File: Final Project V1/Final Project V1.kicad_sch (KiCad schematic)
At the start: 51 parts, among them J1 39299043, J2 Conn_02x03_Counter_Clockwise, J3 Conn_02x02_Counter_Clockwise, J4 Conn_02x01, J5 Conn_02x01, J7 Conn_02x01, J8 75867-132LF, J9 10056845-110LF, Q1 SS8050-G, Q2 SS8050-G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

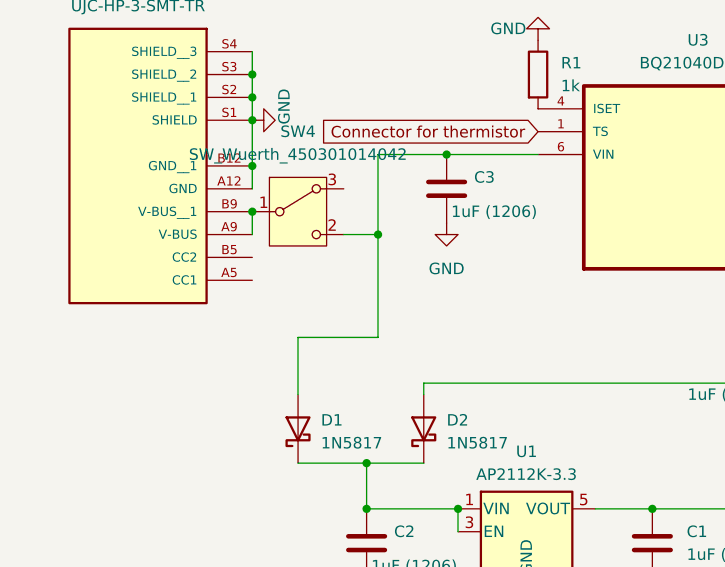
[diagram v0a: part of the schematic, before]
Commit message: Added resistors to control channel on USB-C cause I am a silly goose and didn't do that before
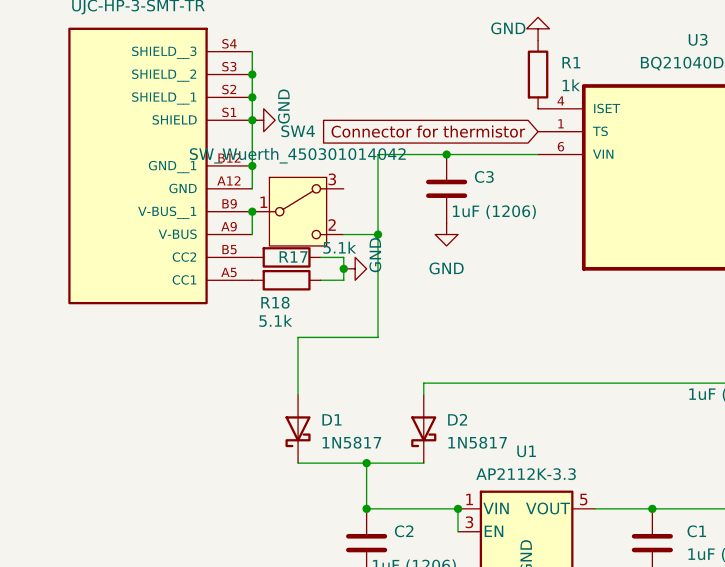
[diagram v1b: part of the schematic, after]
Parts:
- added R17, R18: 5.1k, Resistor_SMD:R_0805_2012Metric_Pad1.20x1.40mm_HandSolder, symbol Device:R
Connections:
- net GND: now also R17.1, R18.1
- net at USB-C1.A5 (CC1): now also R18.2
- net at USB-C1.B5 (CC2): now also R17.2
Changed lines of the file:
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@@
 	)
 	(junction
+		(at 44.45 40.64)
+		(diameter 0)
+		(color 0 0 0 0)
+	)
+	(junction
 		(at 179.07 60.96)
 		(diameter 0)
@@
 	(wire
 		(pts
+			(xy 44.45 41.91) (xy 44.45 40.64)
+		)
+		(stroke
+			(width 0)
+			(type default)
+		)
+	)
+	(wire
+		(pts
 			(xy 199.39 58.42) (xy 201.93 58.42)
 		)
@@
 	(wire
 		(pts
+			(xy 41.91 39.37) (xy 44.45 39.37)
+		)
+		(stroke
+			(width 0)
+			(type default)
+		)
+	)
+	(wire
+		(pts
 			(xy 228.6 74.93) (xy 228.6 80.01)
 		)
@@
 	(wire
 		(pts
+			(xy 41.91 41.91) (xy 44.45 41.91)
+		)
+		(stroke
+			(width 0)
+			(type default)
+		)
+	)
+	(wire
+		(pts
 			(xy 39.37 48.26) (xy 39.37 54.61)
 		)
@@
 	(wire
 		(pts
+			(xy 44.45 39.37) (xy 44.45 40.64)
+		)
+		(stroke
+			(width 0)
+			(type default)
+		)
+	)
+	(wire
+		(pts
 			(xy 243.84 146.05) (xy 246.38 146.05)
 		)
@@
 	)
 	(symbol
+		(lib_id "Device:R")
+		(at 38.1 41.91 270)
+		(unit 1)
+		(exclude_from_sim no)
+		(in_bom yes)
+		(on_board yes)
+		(dnp no)
+		(property "Reference" "R18"
+			(at 36.83 44.45 90)
+			(effects
+				(font
+					(size 1.27 1.27)
+				)
+			)
+		)
+		(property "Value" "5.1k"
+			(at 36.83 46.482 90)
+			(effects
+				(font
+					(size 1.27 1.27)
+				)
+			)
+		)
+		(property "Footprint" "Resistor_SMD:R_0805_2012Metric_Pad1.20x1.40mm_HandSolder"
+			(at 38.1 40.132 90)
+			(effects
+				(font
+					(size 1.27 1.27)
+				)
+				(hide yes)
+			)
+		)
+		(property "Datasheet" "~"
+			(at 38.1 41.91 0)
+			(effects
+				(font
+					(size 1.27 1.27)
+				)
+				(hide yes)
+			)
+		)
+		(property "Description" "Resistor"
+			(at 38.1 41.91 0)
+			(effects
+				(font
+					(size 1.27 1.27)
+				)
+				(hide yes)
+			)
+		)
+		(pin "1"
+		)
+		(pin "2"
+		)
+		(instances
+			(project "Final Project V1"
+				(path "/ac3e449f-fc44-4702-b75e-43cfa6f85799"
+					(reference "R18")
+					(unit 1)
+				)
+			)
+		)
+	)
+	(symbol
 		(lib_id "power:GND")
 		(at 274.32 114.3 0)
@@
 	)
 	(symbol
+		(lib_id "Device:R")
+		(at 38.1 39.37 270)
+		(unit 1)
+		(exclude_from_sim no)
+		(in_bom yes)
+		(on_board yes)
+		(dnp no)
+		(property "Reference" "R17"
+			(at 38.862 39.37 90)
+			(effects
+				(font
+					(size 1.27 1.27)
+				)
+			)
+		)
+		(property "Value" "5.1k"
+			(at 43.942 38.354 90)
+			(effects
+				(font
+					(size 1.27 1.27)
+				)
+			)
+		)
+		(property "Footprint" "Resistor_SMD:R_0805_2012Metric_Pad1.20x1.40mm_HandSolder"
+			(at 38.1 37.592 90)
+			(effects
+				(font
+					(size 1.27 1.27)
+				)
+				(hide yes)
+			)
+		)
+		(property "Datasheet" "~"
+			(at 38.1 39.37 0)
+			(effects
+				(font
+					(size 1.27 1.27)
+				)
+				(hide yes)
+			)
+		)
+		(property "Description" "Resistor"
+			(at 38.1 39.37 0)
+			(effects
+				(font
+					(size 1.27 1.27)
+				)
+				(hide yes)
+			)
+		)
+		(pin "1"
+		)
+		(pin "2"
+		)
+		(instances
+			(project "Final Project V1"
+				(path "/ac3e449f-fc44-4702-b75e-43cfa6f85799"
+					(reference "R17")
+					(unit 1)
+				)
+			)
+		)
+	)
+	(symbol
 		(lib_id "power:GND")
 		(at 64.77 77.47 0)
@@
 					(unit 1)
 				)
+			)
+		)
+	)
+	(symbol
+		(lib_id "power:GND")
+		(at 44.45 40.64 90)
+		(unit 1)
+		(exclude_from_sim no)
+		(in_bom yes)
+		(on_board yes)
+		(dnp no)
+		(property "Reference" "#PWR022"
+			(at 50.8 40.64 0)
+			(effects
+				(font
+					(size 1.27 1.27)
+				)
+				(hide yes)
+			)
+		)
+		(property "Value" "GND"
+			(at 48.006 39.116 0)
+			(effects
+				(font
+					(size 1.27 1.27)
+				)
+			)
+		)
+		(property "Footprint" ""
+			(at 44.45 40.64 0)
+			(effects
+				(font
+					(size 1.27 1.27)
+				)
+				(hide yes)
+			)
+		)
+		(property "Datasheet" ""
+			(at 44.45 40.64 0)
+			(effects
+				(font
+					(size 1.27 1.27)
+				)
+				(hide yes)
+			)
+		)
+		(property "Description" "Power symbol creates a global label with name \"GND\" , ground"
+			(at 44.45 40.64 0)
+			(effects
+				(font
+					(size 1.27 1.27)
+				)
+				(hide yes)
+			)
+		)
+		(pin "1"
+		)
+		(instances
+			(project "Final Project V1"
+				(path "/ac3e449f-fc44-4702-b75e-43cfa6f85799"
+					(reference "#PWR022")
+					(unit 1)
+				)

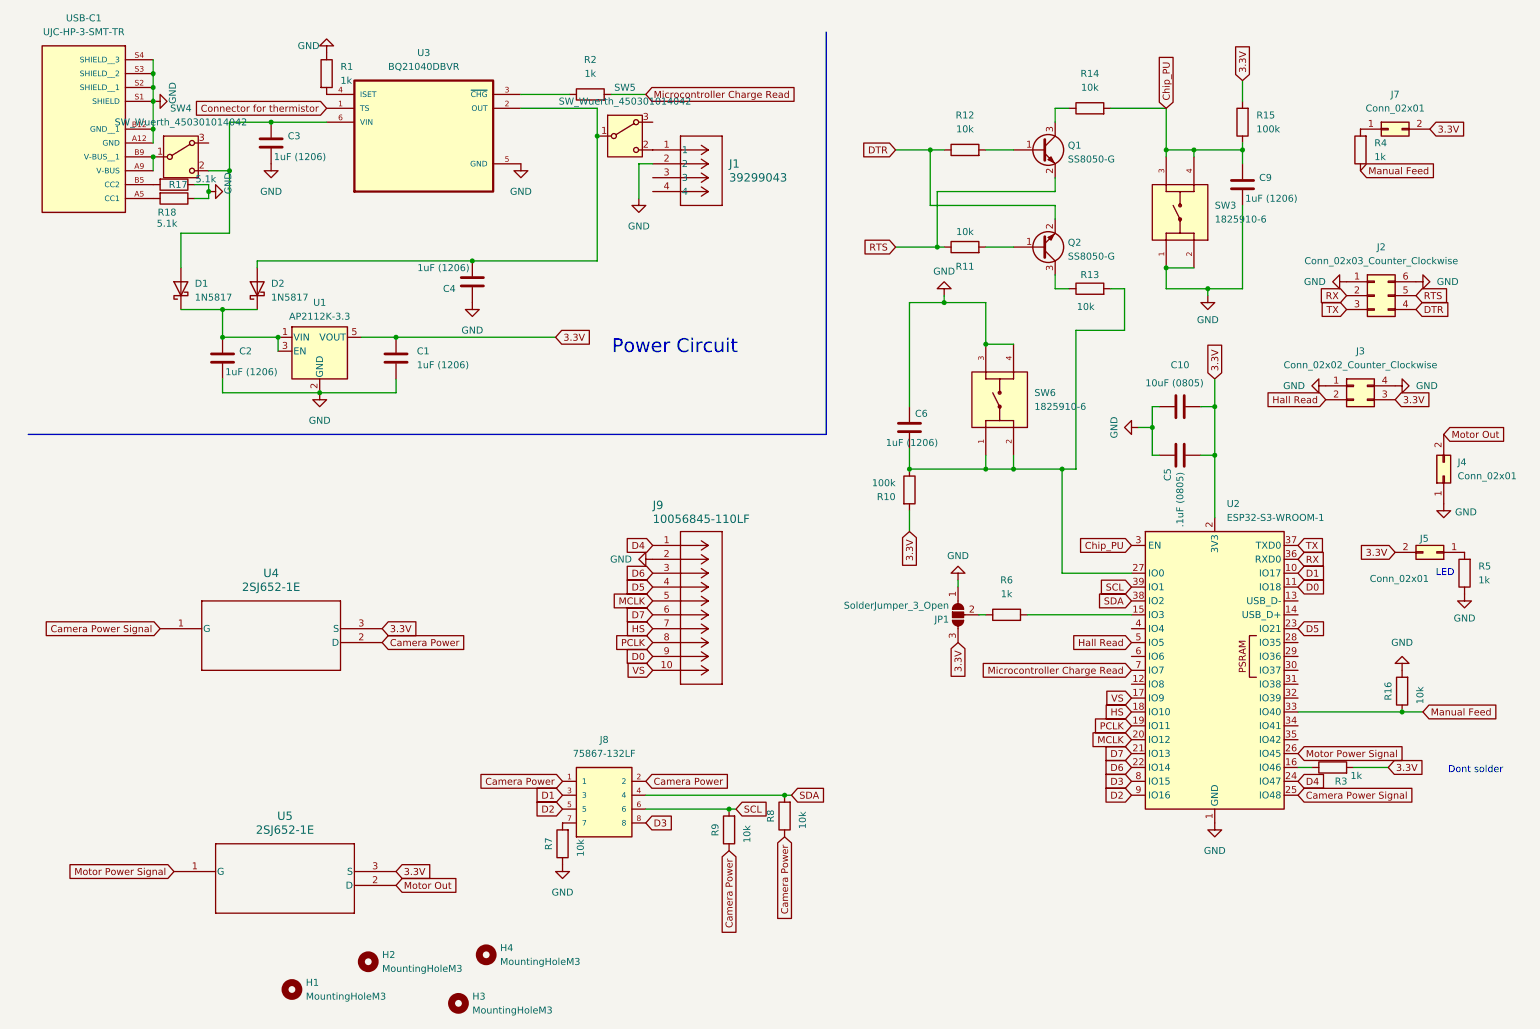
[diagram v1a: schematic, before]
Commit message: V4 Schematic. Will work with V3
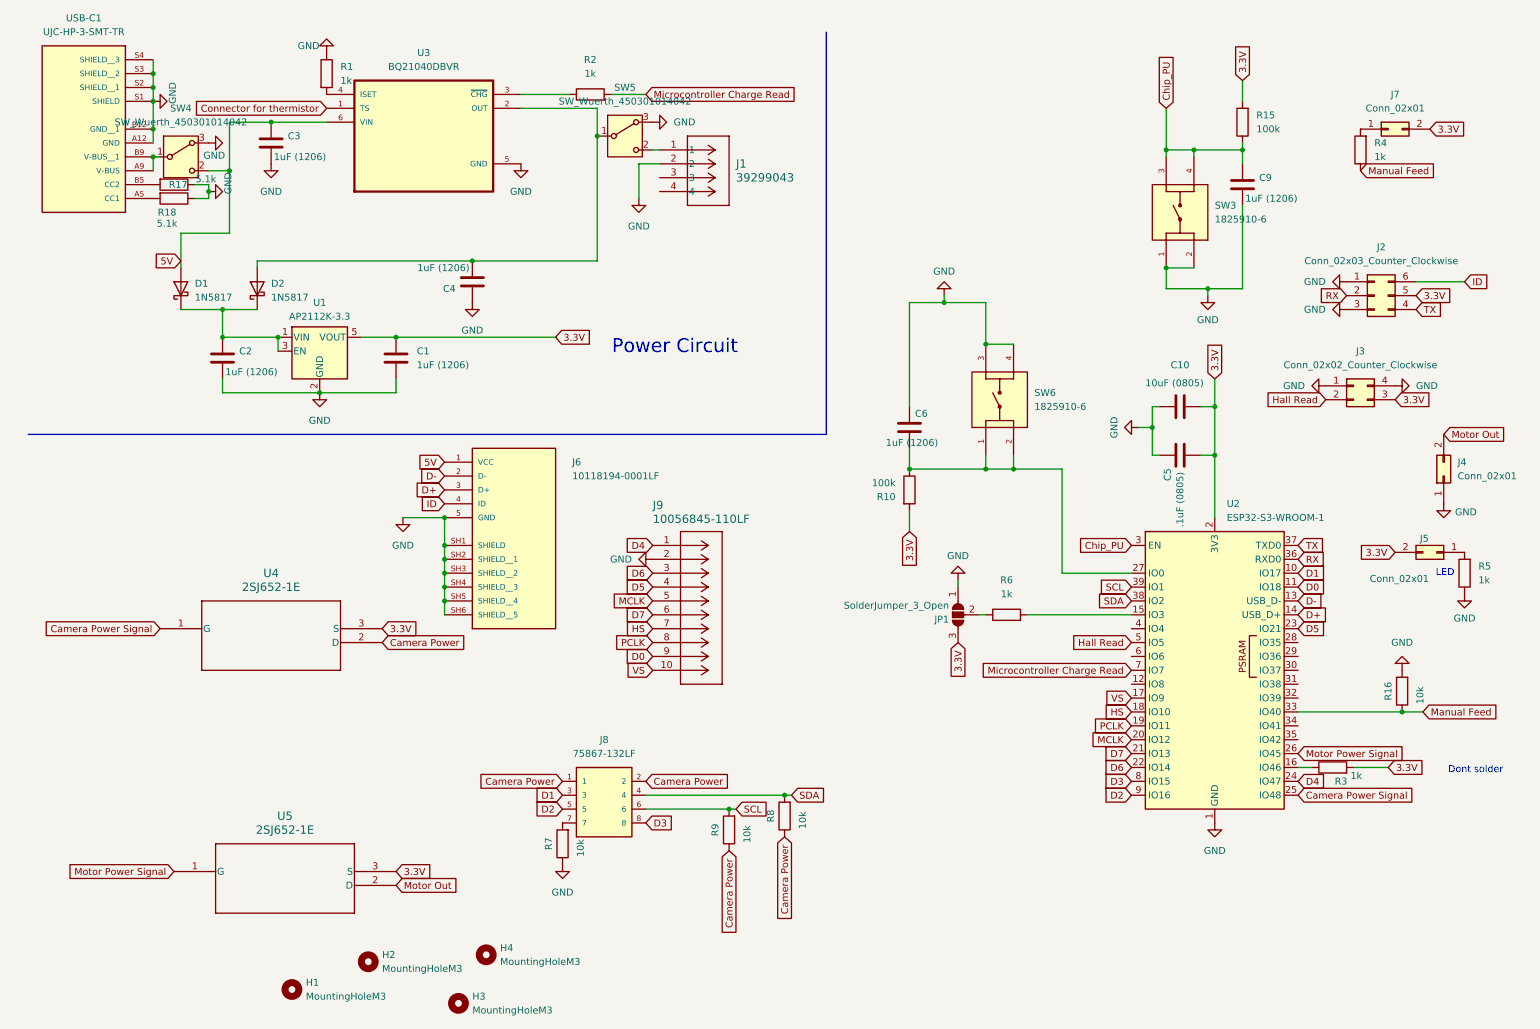
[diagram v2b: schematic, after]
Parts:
- removed Q1, Q2: SS8050-G, Package_TO_SOT_SMD:SOT-23, symbol Device:Q_NPN_BEC
- removed R11, R12, R13, R14: 10k, Resistor_SMD:R_0805_2012Metric_Pad1.20x1.40mm_HandSolder, symbol Device:R
- added J6: 10118194-0001LF, 10118194_0001LF:AMPHENOL_10118194-0001LF, symbol 10118194-0001LF:10118194-0001LF
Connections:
- net DTR is gone; now on net TX: J2.4 (Pin_4)
- net RTS is gone; now on net 3.3V: J2.5 (Pin_5)
- net GND: now also J2.3 (Pin_3), SW4.3 (A), SW5.3 (A), J6.5 (GND), J6.SH1 (SHIELD), J6.SH2 (SHIELD__1), J6.SH3 (SHIELD__2), J6.SH4 (SHIELD__3), J6.SH5 (SHIELD__4), J6.SH6 (SHIELD__5); no longer J2.6 (Pin_6)
- net TX: no longer J2.3 (Pin_3)
- net 5V: now reaches C3.1, D1.2 (A), SW4.2 (C), U3.6 (VIN)
- net 5V: now also J6.1 (VCC)
- net D-: now reaches U2.13 (USB_D-)
- net D-: now also J6.2 (D-)
- net D+: now reaches U2.14 (USB_D+)
- net D+: now also J6.3 (D+)
- new net ID: J2.6 (Pin_6), J6.4 (ID)
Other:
- moved on the sheet: J1
